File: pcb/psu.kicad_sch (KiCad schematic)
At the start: 19 parts, among them J1 Barrel_Jack, U5 LMR16010

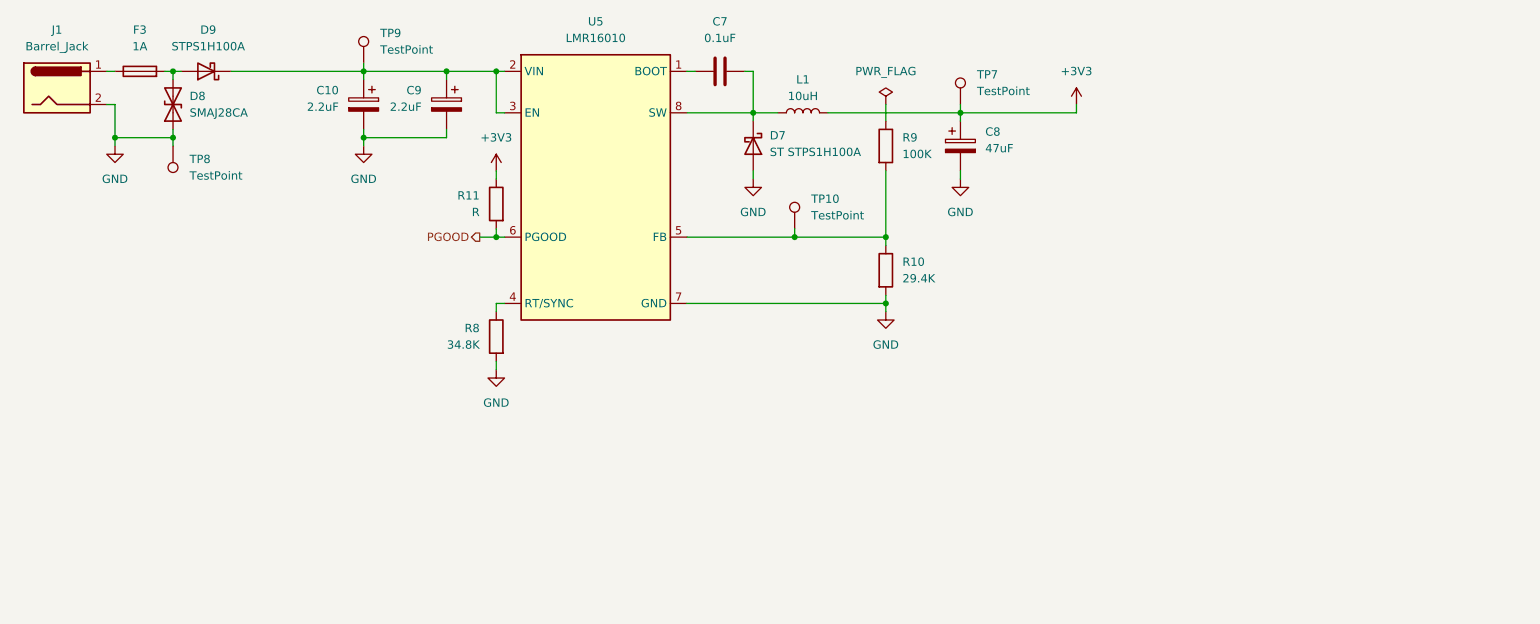
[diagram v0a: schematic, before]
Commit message: feat: add MCU sheet with USB, reset and programming circuitry
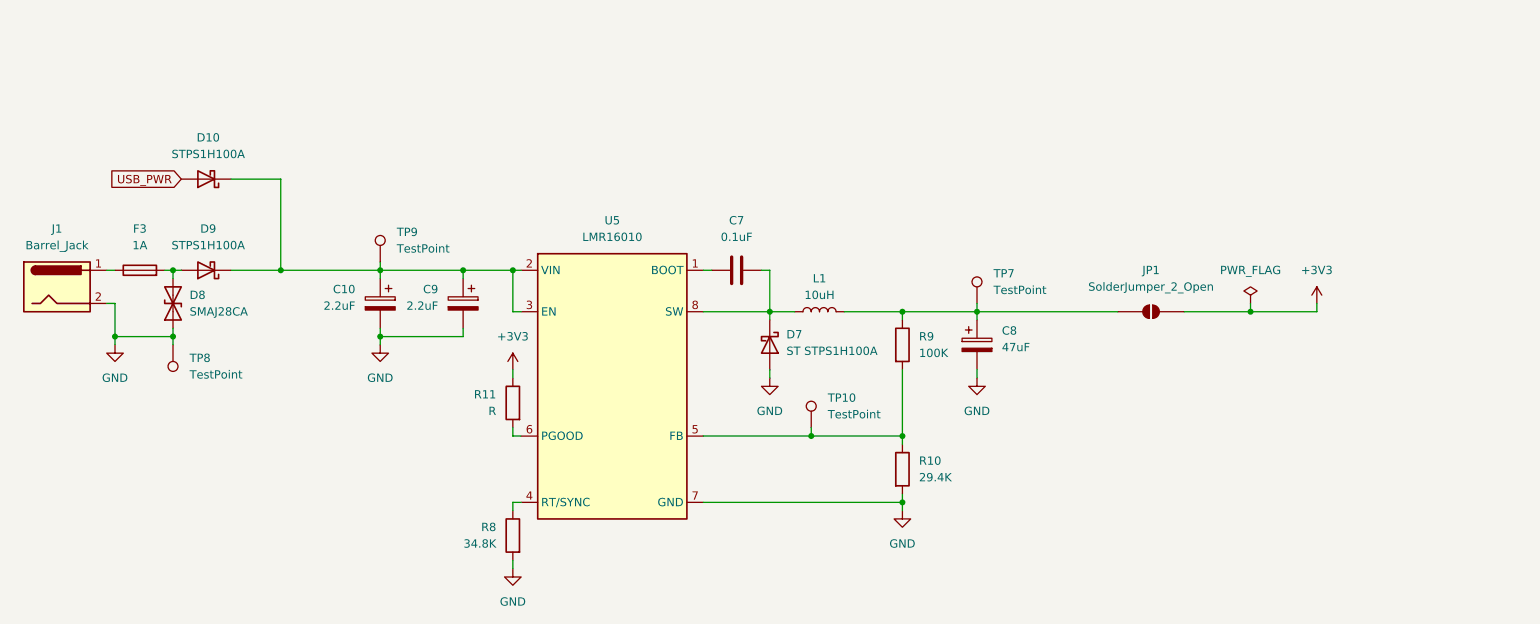
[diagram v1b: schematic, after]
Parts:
- added D10: STPS1H100A, symbol Device:D_Schottky
- added JP1: SolderJumper_2_Open, symbol Jumper:SolderJumper_2_Open
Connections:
- net +3V3: now also JP1.2 (B); no longer C8.1, L1.2, TP7.1
- net at C10.1, C9.1, D9.1 (K)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: now also D10.1 (K)
- net at R9.1: now also C8.1, L1.2, TP7.1, JP1.1 (A)
- net PGOOD: no longer names the net of R11.2, U5.6 (PGOOD)
- new net USB_PWR: D10.2 (A)
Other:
- moved on the sheet: D8, D9, F3, J1, TP8

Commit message: feat: add W5500 ethernet controller
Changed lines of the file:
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@@
+	)
+	(junction
+		(at 140.97 92.71)
+		(diameter 0)
+		(color 0 0 0 0)
 	)
 	(junction
@@
 	)
 	(junction
+		(at 71.12 57.15)
+		(diameter 0)
+		(color 0 0 0 0)
+	)
+	(junction
 		(at 144.78 82.55)
 		(diameter 0)
@@
 	(wire
 		(pts
-			(xy 128.27 92.71) (xy 158.75 92.71)
+			(xy 128.27 92.71) (xy 140.97 92.71)
 		)
 		(stroke
@@
 	(wire
 		(pts
-			(xy 63.5 57.15) (xy 78.74 57.15)
+			(xy 140.97 92.71) (xy 158.75 92.71)
+		)
+		(stroke
+			(width 0)
+			(type default)
+		)
+	)
+	(wire
+		(pts
+			(xy 63.5 57.15) (xy 71.12 57.15)
 		)
 		(stroke
@@
 		(pts
 			(xy 138.43 57.15) (xy 137.16 57.15)
+		)
+		(stroke
+			(width 0)
+			(type default)
+		)
+	)
+	(wire
+		(pts
+			(xy 71.12 57.15) (xy 78.74 57.15)
 		)
 		(stroke
@@
 					(unit 1)
 				)
+			)
+		)
+	)
+	(symbol
+		(lib_id "power:PWR_FLAG")
+		(at 71.12 57.15 0)
+		(unit 1)
+		(body_style 1)
+		(exclude_from_sim no)
+		(in_bom yes)
+		(on_board yes)
+		(in_pos_files yes)
+		(dnp no)
+		(fields_autoplaced yes)
+		(property "Reference" "#FLG08"
+			(at 71.12 55.245 0)
+			(hide yes)
+			(show_name no)
+			(do_not_autoplace no)
+			(effects
+				(font
+					(size 1.27 1.27)
+				)
+			)
+		)
+		(property "Value" "PWR_FLAG"
+			(at 71.12 52.07 0)
+			(show_name no)
+			(do_not_autoplace no)
+			(effects
+				(font
+					(size 1.27 1.27)
+				)
+			)
+		)
+		(property "Footprint" ""
+			(at 71.12 57.15 0)
+			(hide yes)
+			(show_name no)
+			(do_not_autoplace no)
+			(effects
+				(font
+					(size 1.27 1.27)
+				)
+			)
+		)
+		(property "Datasheet" ""
+			(at 71.12 57.15 0)
+			(hide yes)
+			(show_name no)
+			(do_not_autoplace no)
+			(effects
+				(font
+					(size 1.27 1.27)
+				)
+			)
+		)
+		(property "Description" "Special symbol for telling ERC where power comes from"
+			(at 71.12 57.15 0)
+			(hide yes)
+			(show_name no)
+			(do_not_autoplace no)
+			(effects
+				(font
+					(size 1.27 1.27)
+				)
+			)
+		)
+		(pin "1"
+		)
+		(instances
+			(project "EveningStar"
+				(path "/4c61f5a2-f8d4-462a-9bc3-d74437d30372/2e538fbd-4766-4d3c-804f-b602af6e3385"
+					(reference "#FLG08")
+					(unit 1)
+				)
+			)
+		)
+	)
+	(symbol
+		(lib_id "power:PWR_FLAG")
+		(at 140.97 92.71 0)
+		(unit 1)
+		(body_style 1)
+		(exclude_from_sim no)
+		(in_bom yes)
+		(on_board yes)
+		(in_pos_files yes)
+		(dnp no)
+		(fields_autoplaced yes)
+		(property "Reference" "#FLG09"
+			(at 140.97 90.805 0)
+			(hide yes)
+			(show_name no)
+			(do_not_autoplace no)
+			(effects
+				(font
+					(size 1.27 1.27)
+				)
+			)
+		)
+		(property "Value" "PWR_FLAG"
+			(at 140.97 87.63 0)
+			(show_name no)
+			(do_not_autoplace no)
+			(effects
+				(font
+					(size 1.27 1.27)
+				)
+			)
+		)
+		(property "Footprint" ""
+			(at 140.97 92.71 0)
+			(hide yes)
+			(show_name no)
+			(do_not_autoplace no)
+			(effects
+				(font
+					(size 1.27 1.27)
+				)
+			)
+		)
+		(property "Datasheet" ""
+			(at 140.97 92.71 0)
+			(hide yes)
+			(show_name no)
+			(do_not_autoplace no)
+			(effects
+				(font
+					(size 1.27 1.27)
+				)
+			)
+		)
+		(property "Description" "Special symbol for telling ERC where power comes from"
+			(at 140.97 92.71 0)
+			(hide yes)
+			(show_name no)
+			(do_not_autoplace no)
+			(effects
+				(font
+					(size 1.27 1.27)
+				)
+			)
+		)
+		(pin "1"
+		)
+		(instances
+			(project "EveningStar"
+				(path "/4c61f5a2-f8d4-462a-9bc3-d74437d30372/2e538fbd-4766-4d3c-804f-b602af6e3385"
+					(reference "#FLG09")
+					(unit 1)
+				)

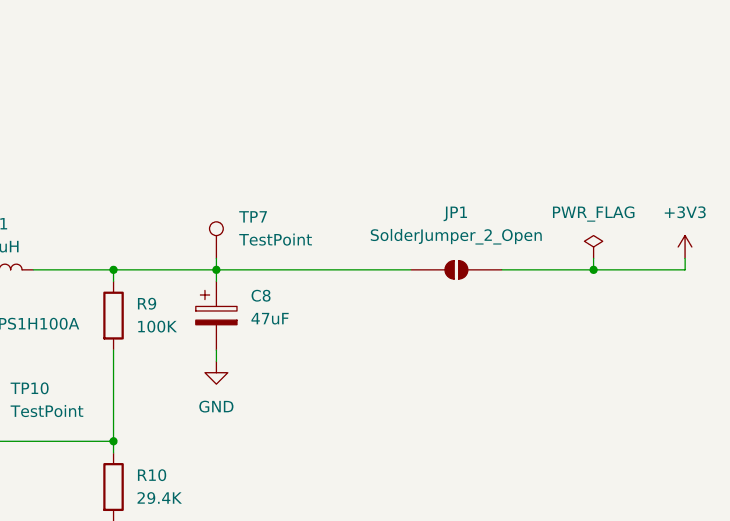
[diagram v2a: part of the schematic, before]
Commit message: feat: connect ethernet to mcu and sort erc errors
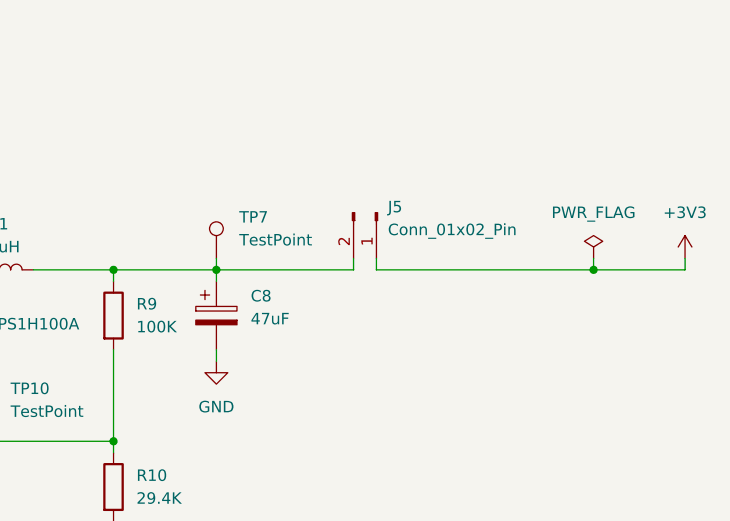
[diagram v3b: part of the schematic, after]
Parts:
- removed JP1: SolderJumper_2_Open, symbol Jumper:SolderJumper_2_Open
- added J5: Conn_01x02_Pin, symbol Connector:Conn_01x02_Pin
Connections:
- net +3V3: now also J5.1 (Pin_1)
- net at C8.1, L1.2, R9.1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: now also J5.2 (Pin_2)
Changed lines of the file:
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@@
+	(wire
+		(pts
+			(xy 187.96 63.5) (xy 212.09 63.5)
+		)
+		(stroke
+			(width 0)
+			(type default)
+		)
+	)
 	(wire
 		(pts
@@
 	(wire
 		(pts
+			(xy 185.42 63.5) (xy 185.42 62.23)
+		)
+		(stroke
+			(width 0)
+			(type default)
+		)
+	)
+	(wire
+		(pts
 			(xy 99.06 92.71) (xy 99.06 93.98)
 		)
@@
 	(wire
 		(pts
+			(xy 170.18 63.5) (xy 185.42 63.5)
+		)
+		(stroke
+			(width 0)
+			(type default)
+		)
+	)
+	(wire
+		(pts
 			(xy 38.1 67.31) (xy 38.1 68.58)
 		)
@@
 	(wire
 		(pts
-			(xy 170.18 63.5) (xy 191.77 63.5)
-		)
-		(stroke
-			(width 0)
-			(type default)
-		)
-	)
-	(wire
-		(pts
 			(xy 78.74 68.58) (xy 78.74 67.31)
 		)
@@
 	(wire
 		(pts
-			(xy 201.93 63.5) (xy 212.09 63.5)
-		)
-		(stroke
-			(width 0)
-			(type default)
-		)
-	)
-	(wire
-		(pts
 			(xy 100.33 92.71) (xy 99.06 92.71)
 		)
@@
 		(pts
 			(xy 170.18 63.5) (xy 170.18 64.77)
+		)
+		(stroke
+			(width 0)
+			(type default)
+		)
+	)
+	(wire
+		(pts
+			(xy 187.96 62.23) (xy 187.96 63.5)
 		)
 		(stroke
@@
 	)
 	(symbol
-		(lib_id "Jumper:SolderJumper_2_Open")
-		(at 196.85 63.5 0)
-		(unit 1)
-		(body_style 1)
-		(exclude_from_sim no)
-		(in_bom no)
-		(on_board yes)
-		(in_pos_files yes)
-		(dnp no)
-		(fields_autoplaced yes)
-		(property "Reference" "JP1"
-			(at 196.85 57.15 0)
-			(show_name no)
-			(do_not_autoplace no)
-			(effects
-				(font
-					(size 1.27 1.27)
-				)
-			)
-		)
-		(property "Value" "SolderJumper_2_Open"
-			(at 196.85 59.69 0)
-			(show_name no)
-			(do_not_autoplace no)
-			(effects
-				(font
-					(size 1.27 1.27)
-				)
-			)
-		)
-		(property "Footprint" ""
-			(at 196.85 63.5 0)
-			(hide yes)
-			(show_name no)
-			(do_not_autoplace no)
-			(effects
-				(font
-					(size 1.27 1.27)
-				)
-			)
-		)
-		(property "Datasheet" ""
-			(at 196.85 71.12 0)
-			(hide yes)
-			(show_name no)
-			(do_not_autoplace no)
-			(effects
-				(font
-					(size 1.27 1.27)
-				)
-			)
-		)
-		(property "Description" "Solder Jumper, 2-pole, open"
-			(at 196.85 68.58 0)
-			(hide yes)
-			(show_name no)
-			(do_not_autoplace no)
-			(effects
-				(font
-					(size 1.27 1.27)
-				)
-			)
-		)
-		(pin "2"
-		)
-		(pin "1"
-		)
-		(instances
-			(project "EveningStar"
-				(path "/4c61f5a2-f8d4-462a-9bc3-d74437d30372/2e538fbd-4766-4d3c-804f-b602af6e3385"
-					(reference "JP1")
-					(unit 1)
-				)
-			)
-		)
-	)
-	(symbol
 		(lib_id "Device:L")
 		(at 146.05 63.5 90)
@@
 					(unit 1)
 				)
+			)
+		)
+	)
+	(symbol
+		(lib_id "Connector:Conn_01x02_Pin")
+		(at 187.96 57.15 270)
+		(unit 1)
+		(body_style 1)
+		(exclude_from_sim no)
+		(in_bom yes)
+		(on_board yes)
+		(in_pos_files yes)
+		(dnp no)
+		(fields_autoplaced yes)
+		(property "Reference" "J5"
+			(at 189.23 56.5149 90)
+			(show_name no)
+			(do_not_autoplace no)
+			(effects
+				(font
+					(size 1.27 1.27)
+				)
+				(justify left)
+			)
+		)
+		(property "Value" "Conn_01x02_Pin"
+			(at 189.23 59.0549 90)
+			(show_name no)
+			(do_not_autoplace no)
+			(effects
+				(font
+					(size 1.27 1.27)
+				)
+				(justify left)
+			)
+		)
+		(property "Footprint" ""
+			(at 187.96 57.15 0)
+			(hide yes)
+			(show_name no)
+			(do_not_autoplace no)
+			(effects
+				(font
+					(size 1.27 1.27)
+				)
+			)
+		)
+		(property "Datasheet" ""
+			(at 187.96 57.15 0)
+			(hide yes)
+			(show_name no)
+			(do_not_autoplace no)
+			(effects
+				(font
+					(size 1.27 1.27)
+				)
+			)
+		)
+		(property "Description" "Generic connector, single row, 01x02, script generated"
+			(at 187.96 57.15 0)
+			(hide yes)
+			(show_name no)
+			(do_not_autoplace no)
+			(effects
+				(font
+					(size 1.27 1.27)
+				)
+			)
+		)
+		(pin "2"
+		)
+		(pin "1"
+		)
+		(instances
+			(project "EveningStar"
+				(path "/4c61f5a2-f8d4-462a-9bc3-d74437d30372/2e538fbd-4766-4d3c-804f-b602af6e3385"
+					(reference "J5")
+					(unit 1)
+				)

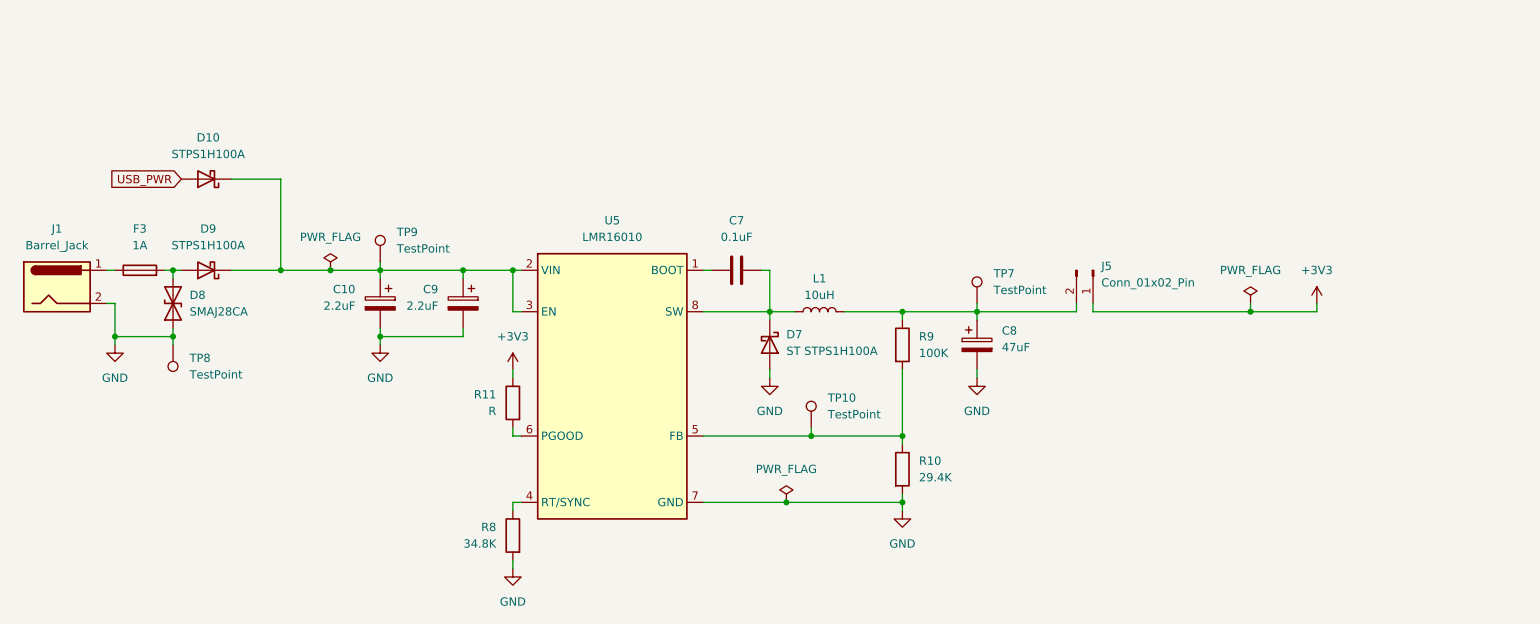
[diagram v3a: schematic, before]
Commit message: feat: update compoents with lcsc parts
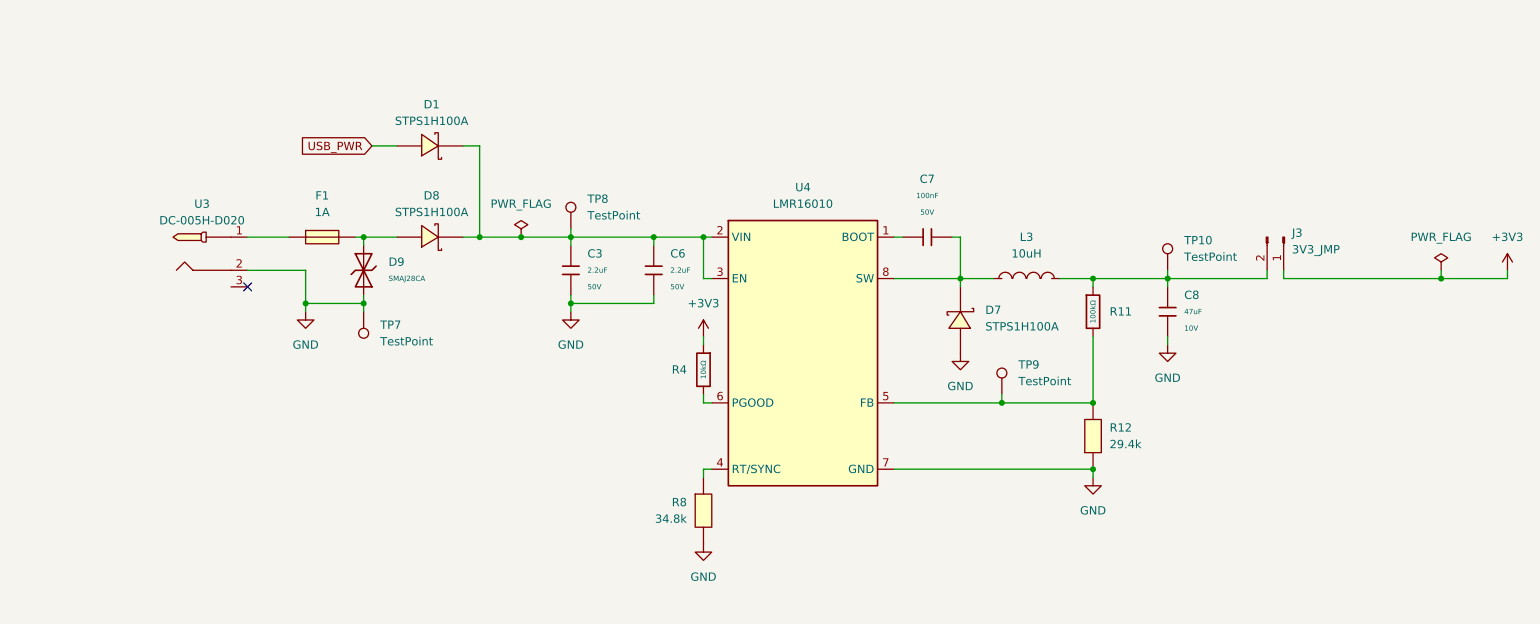
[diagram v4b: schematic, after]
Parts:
- removed C10, C9: 2.2uF, symbol Device:C_Polarized
- removed C7: 0.1uF, symbol Device:C
- removed C8: 47uF, symbol Device:C_Polarized
- removed D10, D9: STPS1H100A, symbol Device:D_Schottky
- removed D7: ST STPS1H100A, symbol Device:D_Schottky
- removed D8: SMAJ28CA, symbol Device:D_TVS
- removed F3: 1A, symbol Device:Fuse
- removed J1: Barrel_Jack, symbol Connector:Barrel_Jack
- removed L1: 10uH, symbol Device:L
- removed R10: 29.4K, symbol Device:R
- removed R11: R, symbol Device:R
- removed R8: 34.8K, symbol Device:R
- removed R9: 100K, symbol Device:R
- added C3, C6: 2.2uF, PCM_JLCPCB:C_1206, symbol PCM_JLCPCB-Capacitors:1206,2.2uF
- added C7: 100nF, PCM_JLCPCB:C_0603, symbol PCM_JLCPCB-Capacitors:0603,100nF
- added C8: 47uF, PCM_JLCPCB:C_1206, symbol PCM_JLCPCB-Capacitors:1206,47uF
- added D1, D7, D8: STPS1H100A, EasyEDA:SMA_L4.3-W2.6-LS5.2-RD, symbol EasyEDA:STPS1H100A
- added D9: SMAJ28CA, PCM_JLCPCB:D_SMA, symbol PCM_JLCPCB-Diodes:TVS-Bi,SMAJ28CA
- added F1: 1A, EasyEDA:F1206, symbol EasyEDA:BSMD1206C-1100T
- added L3: 10uH, EasyEDA:IND-SMD_L4.0-W4.0_FNR40XXS, symbol EasyEDA:FNR4030S100MT
- added R11: 100kΩ, PCM_JLCPCB:R_0603, symbol PCM_JLCPCB-Resistors:0603,100kΩ
- added R12: 29.4k, EasyEDA:R0603, symbol EasyEDA:FRC0603F2942TS
- added R4: 10kΩ, PCM_JLCPCB:R_0603, symbol PCM_JLCPCB-Resistors:0603,10kΩ
- added R8: 34.8k, EasyEDA:R0603, symbol EasyEDA:FRC0603F3482TS
- added U3: DC-005H-D020, EasyEDA:DC-IN-TH_G-SWITCH_DC-005H-D020, symbol EasyEDA:DC-005H-D020
- J3: renamed from J5; value Conn_01x02_Pin -> 3V3_JMP; footprint (none) -> EasyEDA:HDR-TH_2P-P2.54-V-M; LSCS Part (none) -> C492401; MPN (none) -> PZ254V-11-02P
- TP10: renamed from TP7; footprint (none) -> EasyEDA:TEST-TH_BD2.54-P1.4_BLACK; LCSC Part (none) -> C5199801; MPN (none) -> RH-5001
- TP7: renamed from TP8; footprint (none) -> EasyEDA:TEST-TH_BD2.54-P1.4_BLACK; LCSC Part (none) -> C5199801; MPN (none) -> RH-5001
- TP8: renamed from TP9; footprint (none) -> EasyEDA:TEST-TH_BD2.54-P1.4_BLACK; LCSC Part (none) -> C5199801; MPN (none) -> RH-5001
- TP9: renamed from TP10; footprint (none) -> EasyEDA:TEST-TH_BD2.54-P1.4_BLACK; LCSC Part (none) -> C5199801; MPN (none) -> RH-5001
- U4: renamed from U5; footprint Package_SO:Texas_R-PDSO-G8_EP2.95x4.9mm_Mask2.4x3.1mm -> EasyEDA:SOPOWERPAD-8_L4.9-W3.9-P1.27-LS6.0-BL-EP; LCSC Part (none) -> C183084; MPN (none) -> LMR16010PDDAR
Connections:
- net +3V3: now also R4.1
- net GND: now also C3.2, C6.2, C8.2, D7.2 (A), D9.1, R12.1, R8.2, U3.2
- net USB_PWR: now also D1.2 (A)
- net at TP9.1, U4.5 (FB): now also R11.2, R12.2
- net at TP8.1, U4.2 (VIN), U4.3 (EN): now also C3.1, C6.1, D1.1 (C), D8.1 (C)
- net at J3.2 (Pin_2), TP10.1: now also C8.1, L3.2, R11.1
- net at U4.8 (SW): now also C7.2, D7.1 (C), L3.1
- net at U4.6 (PGOOD): now also R4.2
- net at U4.1 (BOOT): now also C7.1
- net at U4.4 (RT/SYNC): now also R8.1
- new net: D8.2 (A), D9.2, F1.2
- new net: F1.1, U3.1
- no-connect marks 0 -> 1
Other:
- moved on the sheet: J3, TP10, TP7, TP8, TP9, U4
